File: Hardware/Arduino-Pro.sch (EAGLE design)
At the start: 37 parts, among them J1 Digital, J2 Analog, J4 POWER, Q1 RESONATORSMD, U1 ATMEGA328, U2 3.3V

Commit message: Finished design review and checklist
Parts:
- added FRAME2: FRAME-LETTER, SparkFun-Aesthetics:FRAME-LETTER
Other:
- note added: "-Added juicy silk graphics"
- note added: "Changes to v17"
- note added: "Revised by: Marshall Taylor"
- note added: "v17"
- moved on the sheet: R2

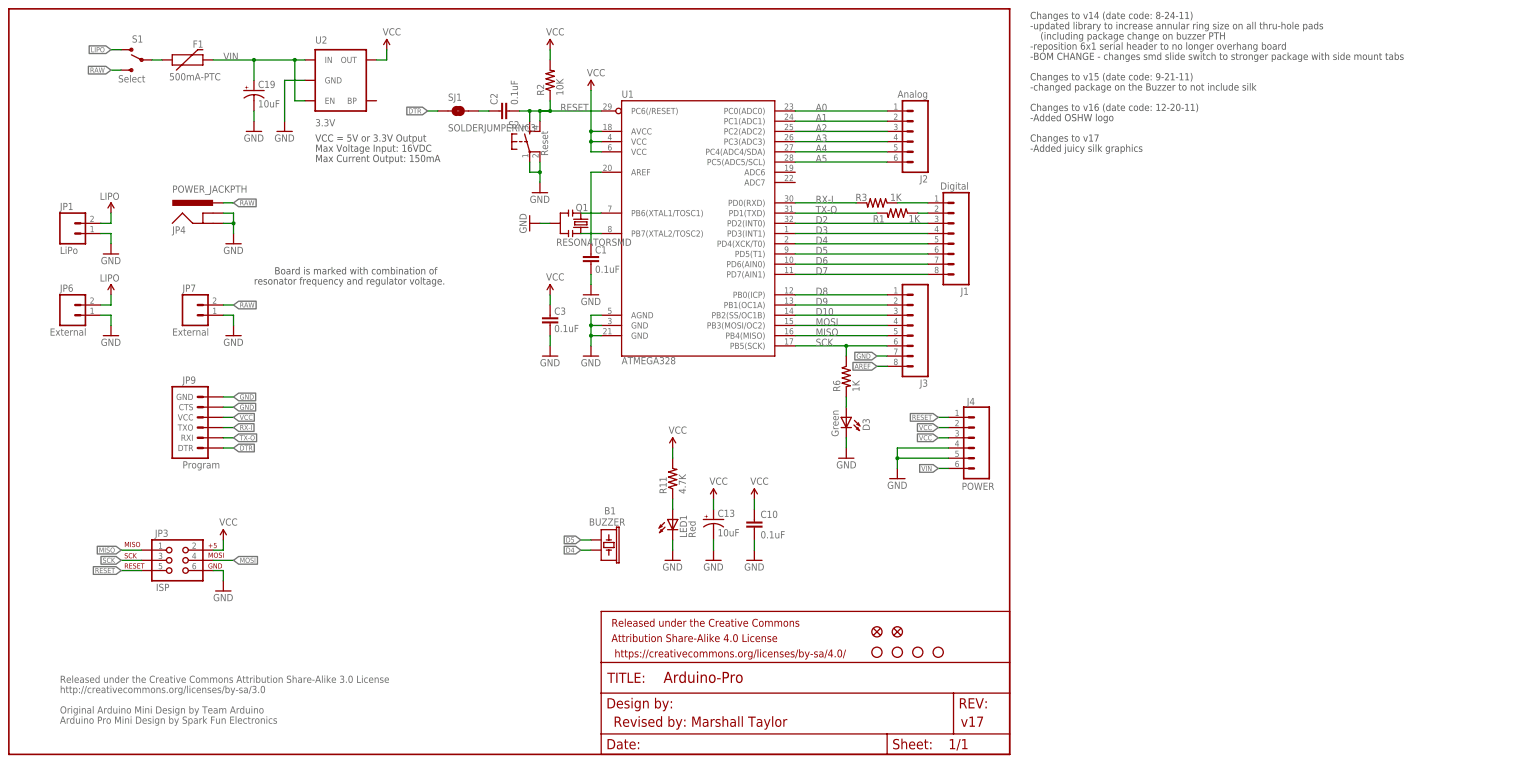
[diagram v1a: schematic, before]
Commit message: Updated schematic to standard, moved rev info to readme
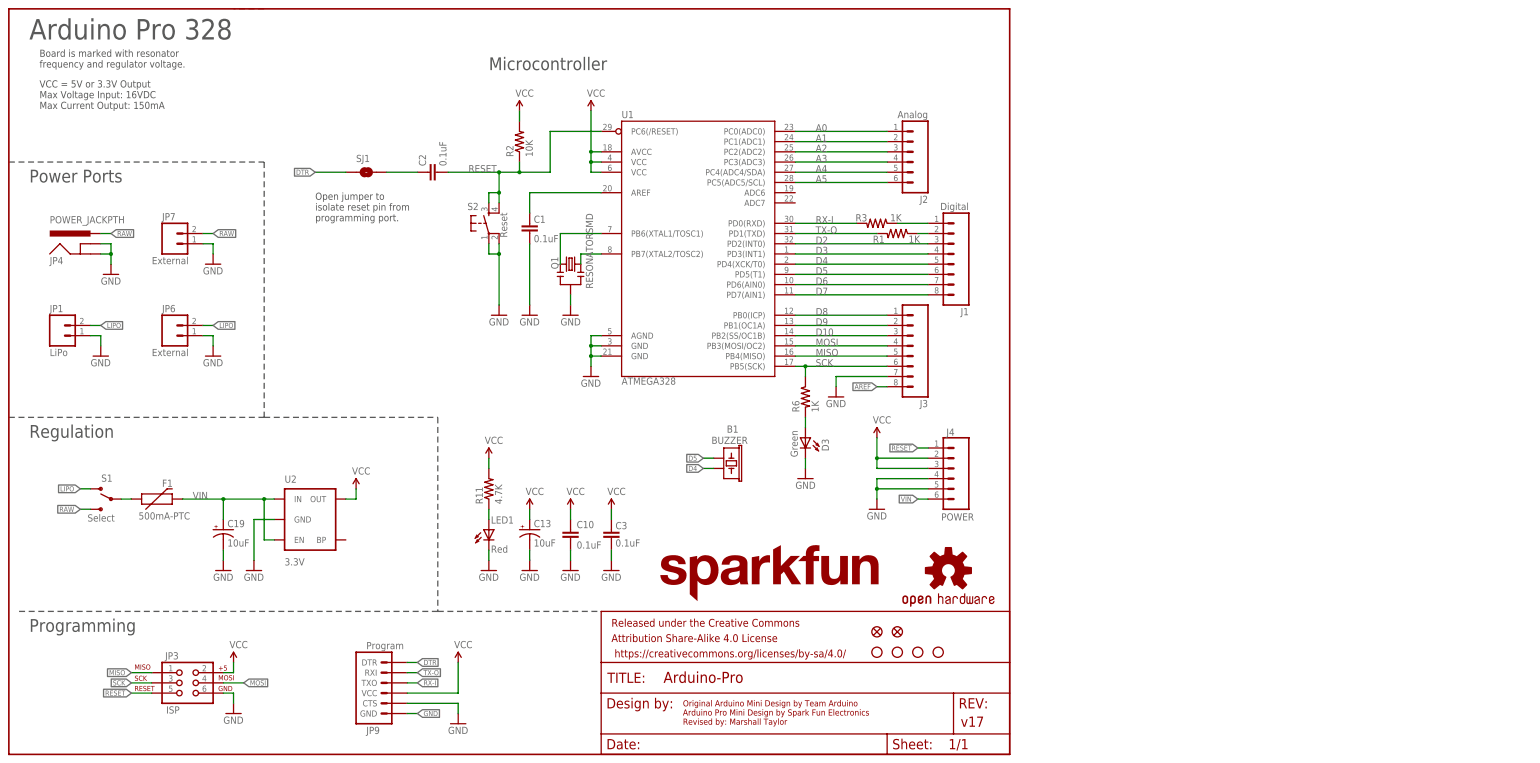
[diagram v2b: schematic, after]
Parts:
- C1, C10, C2, C3: PROD_ID (none) -> CAP-00810
- C13: PROD_ID (none) -> CAP-00811
- D3: PROD_ID (none) -> DIO-00821
- F1: PROD_ID (none) -> RES-08585
- JP1: PROD_ID (none) -> CONN-08352
- JP9: PROD_ID (none) -> CONN-08971
- LED1: PROD_ID (none) -> DIO-00819
- Q1: PROD_ID (none) -> XTAL-08900
- R1, R3, R6: PROD_ID (none) -> RES-07856
- R11: PROD_ID (none) -> RES-07857
- R2: PROD_ID (none) -> RES-00824
- S1: PROD_ID (none) -> SWCH-10651
- S2: PROD_ID (none) -> SWCH-08247
- U1: PROD_ID (none) -> IC-09069
- U2: PROD_ID (none) -> VREG-00823
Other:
- note added: "Arduino Pro 328"
- note added: "Board is marked with resonator frequency and regulator voltage."
- note added: "Microcontroller"
- note added: "Open jumper to isolate reset pin from programming port."
- note added: "Original Arduino Mini Design by Team Arduino Arduino Pro Mini Design by Spark Fun Electronics Revised by: Marshall Taylor"
- note added: "Power Ports"
- note added: "Programming"
- note added: "Regulation"
- note added: "VCC = 5V or 3.3V Output Max Voltage Input: 16VDC Max Current Output: 150mA"
- note removed: "(including package change on buzzer PTH"
- note removed: "-Added OSHW logo"
- note removed: "-Added juicy silk graphics"
- note removed: "-BOM CHANGE - changes smd slide switch to stronger package with side mount tabs"
- note removed: "-changed package on the Buzzer to not include silk"
- note removed: "-reposition 6x1 serial header to no longer overhang board"
- note removed: "-updated library to increase annular ring size on all thru-hole pads"
- note removed: "Arduino Pro Mini Design by Spark Fun Electronics"
- note removed: "Board is marked with combination of"
- note removed: "Changes to v14 (date code: 8-24-11)"
- note removed: "Changes to v15 (date code: 9-21-11)"
- note removed: "Changes to v16 (date code: 12-20-11)"
- note removed: "Changes to v17"
- note removed: "Max Current Output: 150mA"
- note removed: "Max Voltage Input: 16VDC"
- note removed: "Original Arduino Mini Design by Team Arduino"
- note removed: "Released under the Creative Commons Attribution Share-Alike 3.0 License"
- note removed: "Revised by: Marshall Taylor"
- note removed: "VCC = 5V or 3.3V Output"
- note removed: "http://creativecommons.org/licenses/by-sa/3.0"
- note removed: "resonator frequency and regulator voltage."
- moved on the sheet: B1, C1, C10, C13, C19, C2, C3, D3, F1, J1, J2, J3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

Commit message: Fixed schematic issues
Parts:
- Q1: value RESONATORSMD -> 8/16MHz
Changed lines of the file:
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@@
 <attribute name="PROD_ID" value="RES-07856"/>
 </part>
-<part name="Q1" library="SparkFun" deviceset="RESONATOR" device="SMD">
+<part name="Q1" library="SparkFun" deviceset="RESONATOR" device="SMD" value="8/16MHz">
 <attribute name="PROD_ID" value="XTAL-08900"/>
 </part>
@@
 </instance>
 <instance part="Q1" gate="G$1" x="139.7" y="121.92" smashed="yes" rot="MR0">
-<attribute name="NAME" x="136.652" y="120.65" size="1.778" layer="95" font="vector" rot="R90"/>
-<attribute name="VALUE" x="145.288" y="115.824" size="1.778" layer="96" font="vector" rot="R90"/>
+<attribute name="NAME" x="144.272" y="120.65" size="1.778" layer="95" font="vector" rot="R90"/>
+<attribute name="VALUE" x="135.128" y="113.284" size="1.778" layer="96" font="vector" rot="R90"/>
 <attribute name="PROD_ID" x="139.7" y="121.92" size="1.27" layer="96" font="vector" rot="MR0" display="off"/>
 </instance>
@@
 </instance>
 <instance part="JP9" gate="G$1" x="93.98" y="17.78" smashed="yes" rot="MR180">
-<attribute name="VALUE" x="88.9" y="27.94" size="1.778" layer="96" font="vector" rot="MR180"/>
+<attribute name="VALUE" x="86.36" y="27.94" size="1.778" layer="96" font="vector" rot="MR180"/>
 <attribute name="NAME" x="88.9" y="6.858" size="1.778" layer="95" font="vector" rot="MR180"/>
 <attribute name="PROD_ID" x="93.98" y="17.78" size="1.27" layer="96" font="vector" rot="MR180" display="off"/>
@@
 <attribute name="VALUE" x="214.884" y="82.296" size="1.778" layer="96" font="vector"/>
 </instance>
-<instance part="GND12" gate="1" x="111.76" y="7.62" smashed="yes">
-<attribute name="VALUE" x="109.22" y="5.08" size="1.778" layer="96" font="vector"/>
+<instance part="GND12" gate="1" x="109.22" y="5.08" smashed="yes">
+<attribute name="VALUE" x="106.68" y="2.54" size="1.778" layer="96" font="vector"/>
 </instance>
-<instance part="P+3" gate="1" x="111.76" y="22.86" smashed="yes">
-<attribute name="VALUE" x="110.744" y="26.416" size="1.778" layer="96" font="vector"/>
+<instance part="P+3" gate="1" x="109.22" y="25.4" smashed="yes">
+<attribute name="VALUE" x="108.204" y="28.956" size="1.778" layer="96" font="vector"/>
 </instance>
 </instances>
@@
 </segment>
 <segment>
-<wire x1="99.06" y1="12.7" x2="111.76" y2="12.7" width="0.1524" layer="91"/>
-<wire x1="111.76" y1="12.7" x2="111.76" y2="10.16" width="0.1524" layer="91"/>
+<wire x1="99.06" y1="12.7" x2="109.22" y2="12.7" width="0.1524" layer="91"/>
+<wire x1="109.22" y1="12.7" x2="109.22" y2="10.16" width="0.1524" layer="91"/>
 <pinref part="JP9" gate="G$1" pin="CTS"/>
 <pinref part="GND12" gate="1" pin="GND"/>
-</segment>
-<segment>
-<wire x1="99.06" y1="10.16" x2="101.6" y2="10.16" width="0.1524" layer="91"/>
-<label x="101.6" y="10.16" size="1.27" layer="95" font="vector" rot="MR180" xref="yes"/>
+<wire x1="109.22" y1="10.16" x2="109.22" y2="7.62" width="0.1524" layer="91"/>
+<wire x1="99.06" y1="10.16" x2="109.22" y2="10.16" width="0.1524" layer="91"/>
 <pinref part="JP9" gate="G$1" pin="GND"/>
+<junction x="109.22" y="10.16"/>
 </segment>
 <segment>
@@
 </segment>
 <segment>
-<wire x1="99.06" y1="15.24" x2="111.76" y2="15.24" width="0.1524" layer="91"/>
-<wire x1="111.76" y1="15.24" x2="111.76" y2="22.86" width="0.1524" layer="91"/>
+<wire x1="99.06" y1="15.24" x2="109.22" y2="15.24" width="0.1524" layer="91"/>
+<wire x1="109.22" y1="15.24" x2="109.22" y2="25.4" width="0.1524" layer="91"/>
 <pinref part="JP9" gate="G$1" pin="VCC"/>
 <pinref part="P+3" gate="1" pin="VCC"/>

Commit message: Fixed more schematic issues
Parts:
- C19: PROD_ID (none) -> CAP-00811
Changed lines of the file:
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@@
 <attribute name="PROD_ID" value="VREG-00823"/>
 </part>
-<part name="C19" library="SparkFun" deviceset="CAP_POL" device="1206" value="10uF"/>
+<part name="C19" library="SparkFun" deviceset="CAP_POL" device="1206" value="10uF">
+<attribute name="PROD_ID" value="CAP-00811"/>
+</part>
 <part name="GND29" library="SparkFun" deviceset="GND" device=""/>
 <part name="GND30" library="SparkFun" deviceset="GND" device=""/>
@@
 <attribute name="NAME" x="54.356" y="56.515" size="1.778" layer="95" font="vector"/>
 <attribute name="VALUE" x="54.356" y="51.689" size="1.778" layer="96" font="vector"/>
+<attribute name="PROD_ID" x="53.34" y="55.88" size="1.27" layer="96" display="off"/>
 </instance>
 <instance part="GND29" gate="1" x="22.86" y="99.06" smashed="yes">

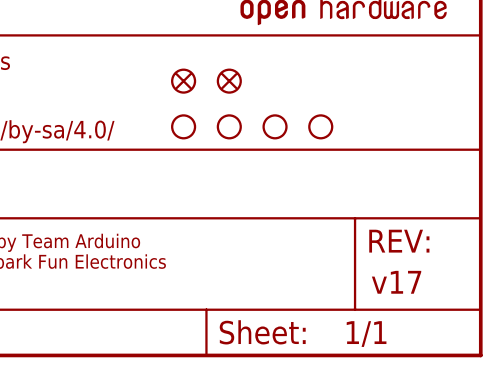
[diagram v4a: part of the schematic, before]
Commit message: Re-imported silk graphics, removed two-pin silk outlines, incremented rev number to 1.8
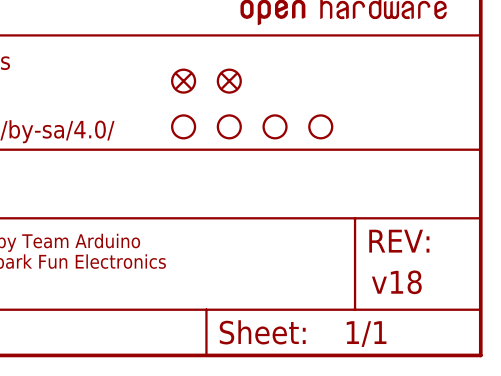
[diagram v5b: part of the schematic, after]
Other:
- note added: "v18"
- note removed: "v17"
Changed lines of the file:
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@@
 <text x="7.62" y="175.26" size="1.778" layer="97" font="vector" align="top-left">Board is marked with resonator
 frequency and regulator voltage.</text>
-<text x="236.728" y="6.858" size="2.54" layer="94" font="vector">v17</text>
+<text x="236.728" y="6.858" size="2.54" layer="94" font="vector">v18</text>
 <text x="167.64" y="13.462" size="1.524" layer="94" font="vector" align="top-left">Original Arduino Mini Design by Team Arduino
 Arduino Pro Mini Design by Spark Fun Electronics

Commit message: Post review and checklist verification
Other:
- note added: "Place 3.3V Reg. for 8MHz Place 5.0V Reg for 16MHz"
- note added: "Place 8MHz XTAL for 3.3V Place 16MHz XTAL for 5.0V"
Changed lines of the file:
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@@
 <text x="5.08" y="78.74" size="3.175" layer="97" font="vector">Regulation</text>
 <text x="5.08" y="30.48" size="3.175" layer="97" font="vector">Programming</text>
-<text x="119.38" y="170.18" size="3.175" layer="97" font="vector">Microcontroller</text>
+<text x="152.4" y="175.26" size="3.175" layer="97" font="vector">Microcontroller</text>
 <wire x1="63.5" y1="83.82" x2="106.68" y2="83.82" width="0.1524" layer="97" style="longdash"/>
 <wire x1="2.54" y1="35.56" x2="106.68" y2="35.56" width="0.1524" layer="97" style="longdash"/>
@@
 isolate reset pin from
 programming port.</text>
+<text x="154.94" y="172.72" size="1.778" layer="97" font="vector" align="top-left">Place 8MHz XTAL for 3.3V
+Place 16MHz XTAL for 5.0V</text>
+<text x="7.62" y="76.2" size="1.778" layer="97" font="vector" align="top-left">Place 3.3V Reg. for 8MHz
+Place 5.0V Reg for 16MHz</text>
 </plain>
 <instances>

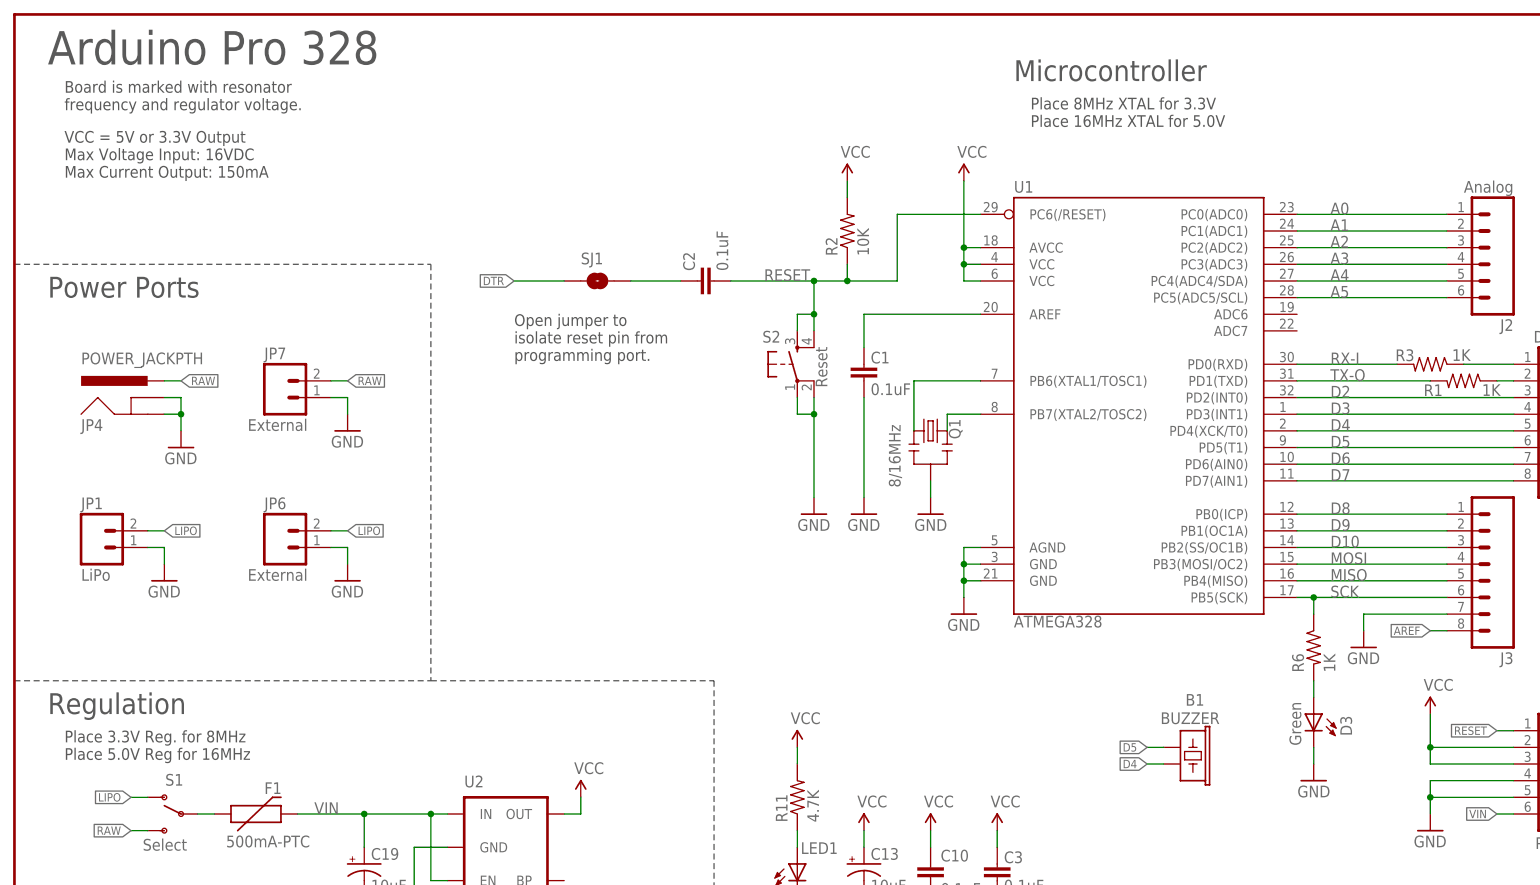
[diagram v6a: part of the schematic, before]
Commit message: Added dual-part SKU information in schematic
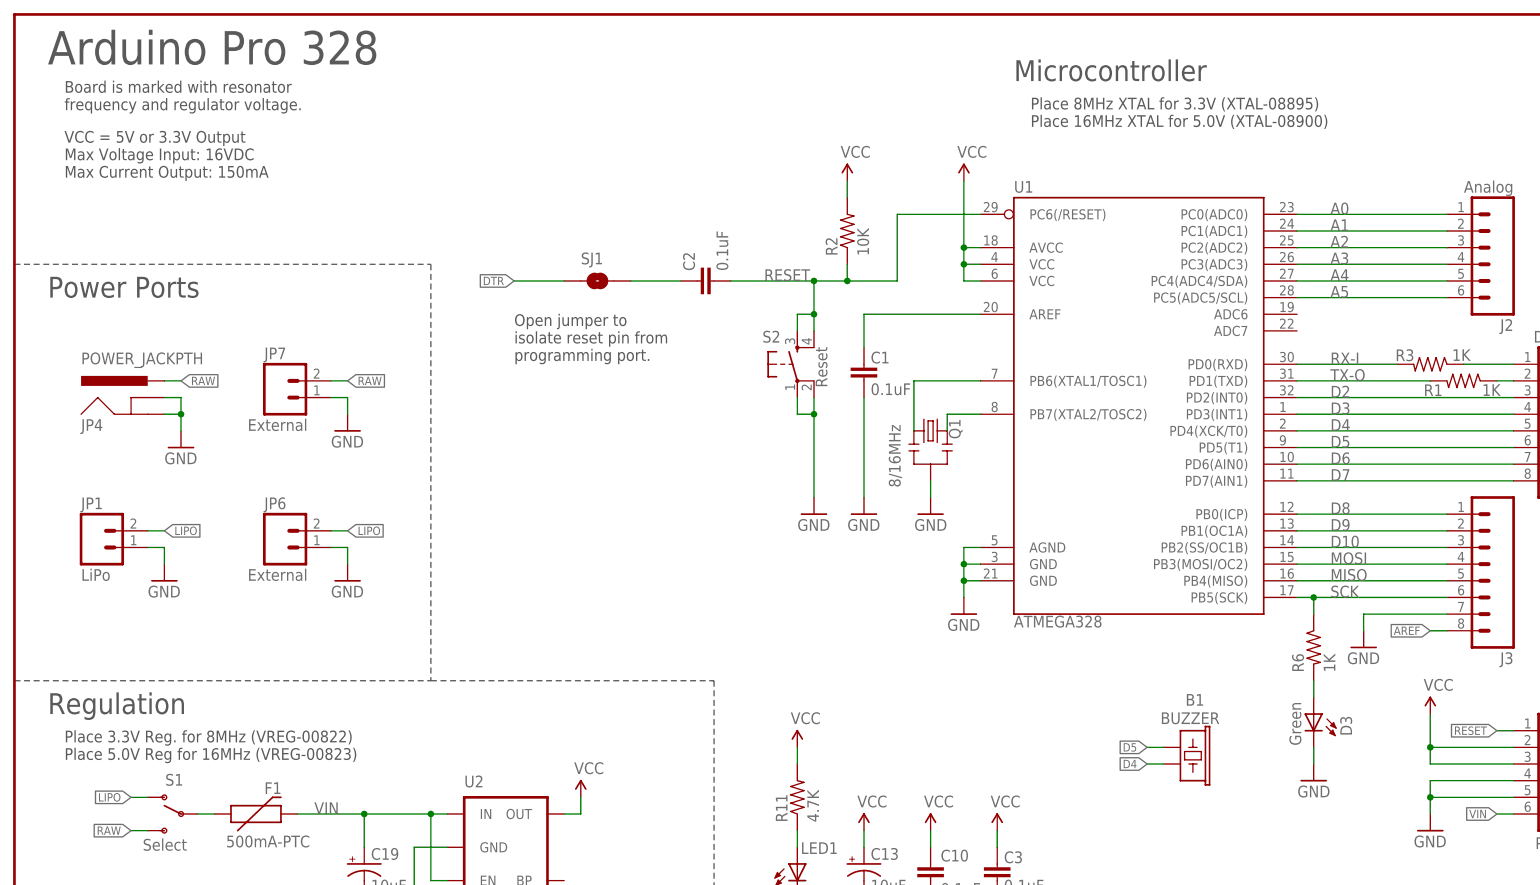
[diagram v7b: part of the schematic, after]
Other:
- note added: "Place 3.3V Reg. for 8MHz (VREG-00822) Place 5.0V Reg for 16MHz (VREG-00823)"
- note added: "Place 8MHz XTAL for 3.3V (XTAL-08895) Place 16MHz XTAL for 5.0V (XTAL-08900)"
- note removed: "Place 3.3V Reg. for 8MHz Place 5.0V Reg for 16MHz"
- note removed: "Place 8MHz XTAL for 3.3V Place 16MHz XTAL for 5.0V"
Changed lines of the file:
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@@
 isolate reset pin from
 programming port.</text>
-<text x="154.94" y="172.72" size="1.778" layer="97" font="vector" align="top-left">Place 8MHz XTAL for 3.3V
-Place 16MHz XTAL for 5.0V</text>
-<text x="7.62" y="76.2" size="1.778" layer="97" font="vector" align="top-left">Place 3.3V Reg. for 8MHz
-Place 5.0V Reg for 16MHz</text>
+<text x="154.94" y="172.72" size="1.778" layer="97" font="vector" align="top-left">Place 8MHz XTAL for 3.3V (XTAL-08895)
+Place 16MHz XTAL for 5.0V (XTAL-08900)</text>
+<text x="7.62" y="76.2" size="1.778" layer="97" font="vector" align="top-left">Place 3.3V Reg. for 8MHz (VREG-00822)
+Place 5.0V Reg for 16MHz (VREG-00823)</text>
 </plain>
 <instances>

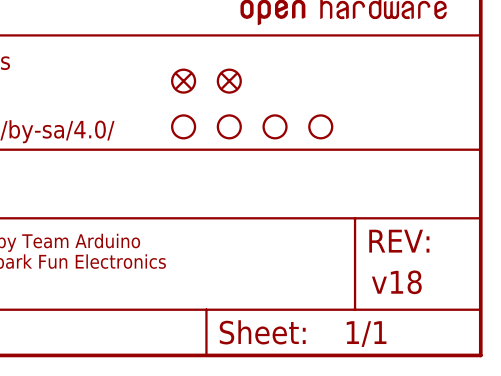
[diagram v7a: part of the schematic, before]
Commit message: Enlarged circles, incremented version number
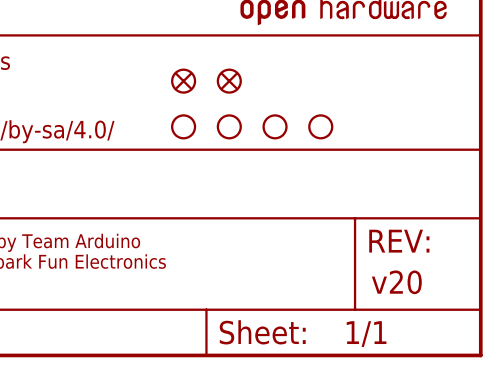
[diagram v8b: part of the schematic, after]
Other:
- note added: "v20"
- note removed: "v18"
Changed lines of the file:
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@@
 <text x="7.62" y="175.26" size="1.778" layer="97" font="vector" align="top-left">Board is marked with resonator
 frequency and regulator voltage.</text>
-<text x="236.728" y="6.858" size="2.54" layer="94" font="vector">v18</text>
+<text x="236.728" y="6.858" size="2.54" layer="94" font="vector">v20</text>
 <text x="167.64" y="13.462" size="1.524" layer="94" font="vector" align="top-left">Original Arduino Mini Design by Team Arduino
 Arduino Pro Mini Design by Spark Fun Electronics
